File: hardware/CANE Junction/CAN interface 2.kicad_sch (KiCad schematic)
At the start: 20 parts, among them J2 glv, U401 TL432DBZ, U402 TPS7B4254, U403 ISO1044BD, U404 ISOM8600, U405 PUCC33420QRAQRQ1

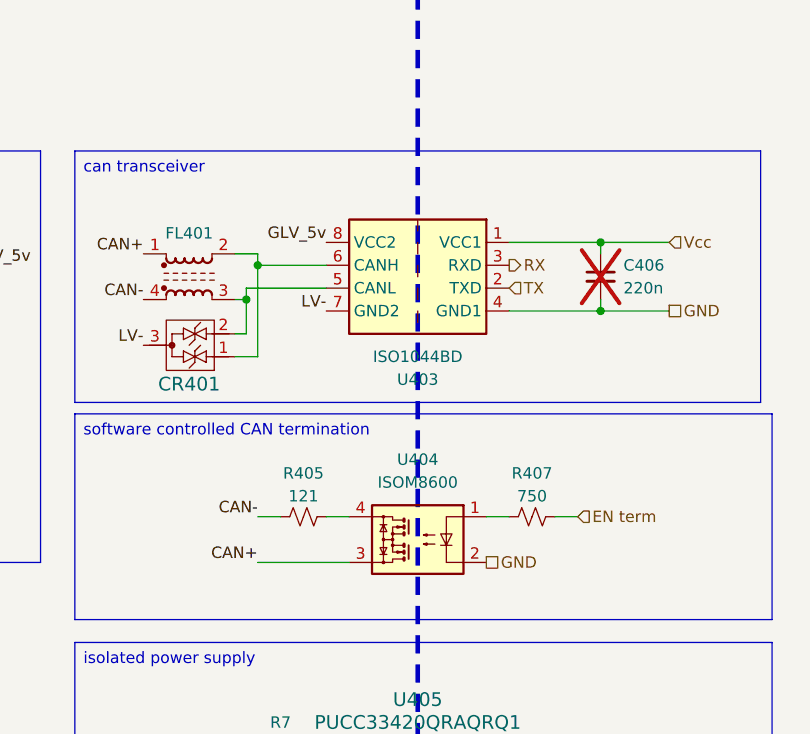
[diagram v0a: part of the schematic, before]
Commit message: transcevier out of stock, swapped out
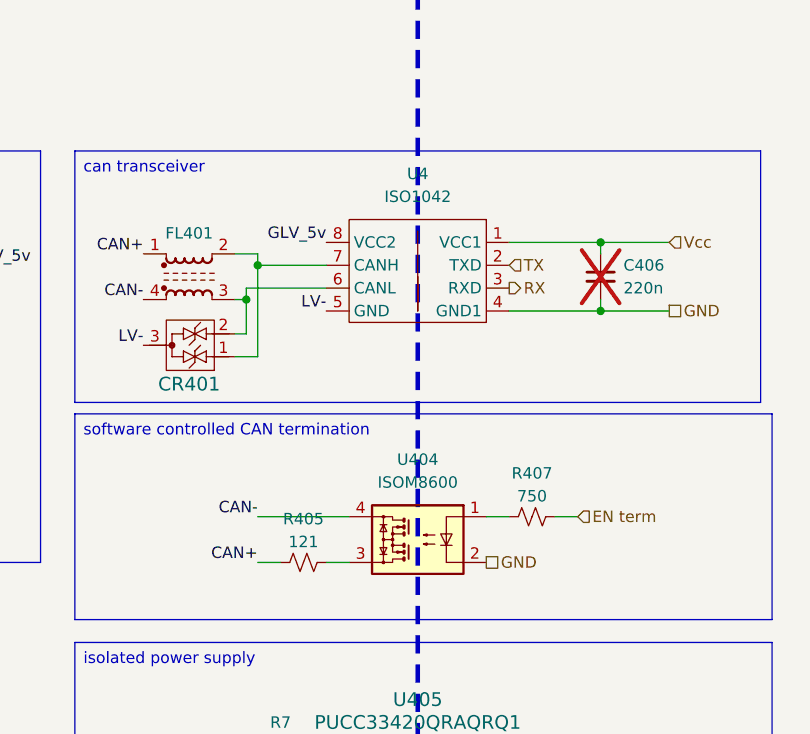
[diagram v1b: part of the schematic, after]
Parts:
- removed U403: ISO1044BD, Package_SO:SOIC-8_5.3x5.3mm_P1.27mm, symbol Interface_CAN_LIN:ISO1044BD
- added U4: ISO1042, Package_SO:SOIC-8_7.5x5.85mm_P1.27mm, symbol zzLocalLibrary:ISO1042
- J2: mouser (none) -> https://www.mouser.com/ProductDetail/Molex/43045-0421?qs=Ue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
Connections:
- net CAN+: now also R405.1; no longer U404.3
- net CAN-: now also U404.4; no longer R405.1
- net GLV_5v: now also U4.8 (VCC2)
- net GND: now also U4.4 (GND1)
- net LV-: now also U4.5 (GND)
- net RX: now also U4.3 (RXD)
- net TX: now also U4.2 (TXD)
- net Vcc: now also U4.1 (VCC1)
- net at R405.2: now also U404.3; no longer U404.4
- net at CR401.2, FL401.3: now also U4.6 (CANL)
- net at CR401.1, FL401.2: now also U4.7 (CANH)
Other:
- moved on the sheet: R405
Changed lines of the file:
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@@
-	(wire
-		(pts
-			(xy 109.22 85.09) (xy 111.76 85.09)
-		)
-		(stroke
-			(width 0)
-			(type default)
-		)
-	)
 	(wire
 		(pts
@@
 	(wire
 		(pts
-			(xy 101.6 85.09) (xy 104.14 85.09)
+			(xy 101.6 85.09) (xy 111.76 85.09)
 		)
 		(stroke
@@
 	(wire
 		(pts
+			(xy 109.22 90.17) (xy 111.76 90.17)
+		)
+		(stroke
+			(width 0)
+			(type default)
+		)
+	)
+	(wire
+		(pts
 			(xy 109.22 120.65) (xy 109.22 123.19)
 		)
@@
 	(wire
 		(pts
-			(xy 101.6 90.17) (xy 111.76 90.17)
+			(xy 101.6 90.17) (xy 104.14 90.17)
 		)
 		(stroke
@@
 	(hierarchical_label "RX"
 		(shape output)
-		(at 129.54 57.15 0)
+		(at 129.54 59.69 0)
 		(effects
 			(font
@@
 	(hierarchical_label "TX"
 		(shape input)
-		(at 129.54 59.69 0)
+		(at 129.54 57.15 0)
 		(effects
 			(font
@@
 	(symbol
 		(lib_id "Device:R_Small_US")
-		(at 106.68 85.09 90)
+		(at 106.68 90.17 90)
 		(unit 1)
 		(body_style 1)
@@
 		(dnp no)
 		(property "Reference" "R405"
-			(at 106.68 80.264 90)
+			(at 106.68 85.344 90)
 			(show_name no)
 			(do_not_autoplace no)
@@
 		)
 		(property "Value" "121"
-			(at 106.68 82.804 90)
+			(at 106.68 87.884 90)
 			(show_name no)
 			(do_not_autoplace no)
@@
 		)
 		(property "Footprint" "Resistor_SMD:R_0805_2012Metric_Pad1.20x1.40mm_HandSolder"
-			(at 106.68 85.09 0)
+			(at 106.68 90.17 0)
 			(hide yes)
 			(show_name no)
@@
 		)
 		(property "Datasheet" ""
-			(at 106.68 85.09 0)
+			(at 106.68 90.17 0)
 			(hide yes)
 			(show_name no)
@@
 		)
 		(property "Description" "Resistor, US symbol"
-			(at 106.68 85.09 0)
+			(at 106.68 90.17 0)
 			(hide yes)
 			(show_name no)
@@
 		)
 		(property "Sim.Device" ""
-			(at 106.68 85.09 0)
+			(at 106.68 90.17 0)
 			(hide yes)
 			(show_name no)
@@
 		)
 		(property "Sim.Type" ""
-			(at 106.68 85.09 0)
+			(at 106.68 90.17 0)
 			(hide yes)
 			(show_name no)
@@
 		)
 		(property "mouser" "https://www.mouser.com/ProductDetail/SEI-Stackpole/RNCP0805FTD121R?qs=sGAEpiMZZMvdGkrng054tyMPH50YnZ95dJmxWK8e%2FBgSyeAIVnAHjA%3D%3D"
-			(at 106.68 85.09 0)
+			(at 106.68 90.17 0)
 			(hide yes)
 			(show_name no)
@@
 		)
 		(property "specs" "121Ohm, 200V, 250mW, 1%, 100ppm, -55C, +155C"
-			(at 106.68 85.09 0)
+			(at 106.68 90.17 0)
 			(hide yes)
 			(show_name no)
@@
 		)
 		(property "unit x1" "0.10"
-			(at 106.68 85.09 0)
+			(at 106.68 90.17 0)
 			(hide yes)
 			(show_name no)
@@
 		)
 		(property "unit x10" "0.012"
-			(at 106.68 85.09 0)
+			(at 106.68 90.17 0)
 			(hide yes)
 			(show_name no)
@@
 		)
 		(property "Sim.Pins" ""
-			(at 106.68 85.09 0)
+			(at 106.68 90.17 0)
 			(hide yes)
 			(show_name no)
@@
 		)
 		(property "note" ""
-			(at 106.68 85.09 0)
+			(at 106.68 90.17 0)
 			(hide yes)
 			(show_name no)
@@
 		)
 		(property "Mouser Part Number" ""
-			(at 106.68 85.09 0)
+			(at 106.68 90.17 0)
 			(hide yes)
 			(show_name no)
@@
 		)
 		(property "Field10" ""
-			(at 106.68 85.09 0)
+			(at 106.68 90.17 0)
 			(hide yes)
 			(show_name no)
@@
 			)
 		)
+		(property "mouser" "https://www.mouser.com/ProductDetail/Molex/43045-0421?qs=UeCeOHRHQebihHCqX%252BVk8Q%3D%3D"
+			(at 29.21 21.59 0)
+			(hide yes)
+			(show_name no)
+			(do_not_autoplace no)
+			(effects
+				(font
+					(size 1.27 1.27)
+				)
+			)
+		)
 		(pin "2"
 		)
@@
 	)
 	(symbol
-		(lib_id "Interface_CAN_LIN:ISO1044BD")
-		(at 119.38 57.15 0)
+		(lib_id "zzLocalLibrary:ISO1042")
+		(at 119.38 50.8 0)
 		(mirror y)
 		(unit 1)
@@
 		(in_pos_files yes)
 		(dnp no)
-		(property "Reference" "U403"
-			(at 119.38 69.85 0)
-			(show_name no)
-			(do_not_autoplace no)
-			(effects
-				(font
-					(size 1.27 1.27)
-				)
-			)
-		)
-		(property "Value" "ISO1044BD"
-			(at 119.38 67.31 0)
-			(show_name no)
-			(do_not_autoplace no)
-			(effects
-				(font
-					(size 1.27 1.27)
-				)
-			)
-		)
-		(property "Footprint" "Package_SO:SOIC-8_5.3x5.3mm_P1.27mm"
-			(at 119.38 67.31 0)
-			(hide yes)
-			(show_name no)
-			(do_not_autoplace no)
-			(effects
-				(font
-					(size 1.27 1.27)
-					(italic yes)
-				)
-			)
-		)
-		(property "Datasheet" "https://www.ti.com/lit/ds/symlink/iso1044.pdf"
-			(at 119.38 69.85 0)
-			(hide yes)
-			(show_name no)
-			(do_not_autoplace no)
-			(effects
-				(font
-					(size 1.27 1.27)
-				)
-			)
-		)
-		(property "Description" "Isolated CAN FD Transceiver, SOIC-8"
-			(at 119.38 57.15 0)
-			(hide yes)
-			(show_name no)
-			(do_not_autoplace no)
-			(effects
-				(font
-					(size 1.27 1.27)
-				)
-			)
+		(property "Reference" "U4"
+			(at 119.38 46.99 0)
+			(show_name no)
+			(do_not_autoplace no)
+			(effects
+				(font
+					(size 1.27 1.27)
+				)
+			)
+		)
+		(property "Value" "ISO1042"
+			(at 119.38 49.53 0)
+			(show_name no)
+			(do_not_autoplace no)
+			(effects
+				(font
+					(size 1.27 1.27)
+				)
+			)
+		)
+		(property "Footprint" "Package_SO:SOIC-8_7.5x5.85mm_P1.27mm"
+			(at 119.38 50.8 0)
+			(hide yes)
+			(show_name no)
+			(do_not_autoplace no)
+			(effects
+				(font
+					(size 1.27 1.27)
+				)
+			)
+		)
+		(property "Datasheet" "https://www.ti.com/lit/ds/symlink/iso1042-q1.pdf"
+			(at 119.38 50.8 0)
+			(hide yes)
+			(show_name no)
+			(do_not_autoplace no)
+			(effects
+				(font
+					(size 1.27 1.27)
+				)
+			)
+		)
+		(property "Description" "isolated can transcevier, 1500Vdc, 5M, CAN-FD"
+			(at 119.38 50.8 0)
+			(hide yes)
+			(show_name no)
+			(do_not_autoplace no)
+			(effects
+				(font
+					(size 1.27 1.27)
+				)
+			)
+		)
+		(property "mouser" "https://www.mouser.com/ProductDetail/Texas-Instruments/ISO1042BQDWVRQ1?qs=byeeYqUIh0NmbePKADUcRQ%3D%3D"
+			(at 119.38 50.8 0)
+			(hide yes)
+			(show_name no)
+			(do_not_autoplace no)
+			(effects
+				(font
+					(size 1.27 1.27)
+				)
+			)
+		)
+		(pin "6"
+		)
+		(pin "4"
+		)
+		(pin "5"
+		)
+		(pin "8"
+		)
+		(pin "2"
 		)
 		(pin "3"
 		)
-		(pin "4"
+		(pin "7"
 		)
 		(pin "1"
-		)
-		(pin "8"
-		)
-		(pin "6"
-		)
-		(pin "7"
-		)
-		(pin "2"
-		)
-		(pin "5"
 		)
 		(instances
 			(project "CANE Junction"
 				(path "/20ac6af0-79b5-4ba6-aad3-75081d02c913/77ba9f55-a932-4615-96e7-79448df1d300"
-					(reference "U403")
+					(reference "U4")
 					(unit 1)
 				)

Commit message: mmm
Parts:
- removed C401, C402, C403, C406, C407: 220n, Capacitor_SMD:C_0805_2012Metric_Pad1.18x1.45mm_HandSolder, symbol Device:C_Small
- removed C404, C405: 22u, Capacitor_SMD:C_0805_2012Metric_Pad1.18x1.45mm_HandSolder, symbol Device:C_Small
- removed CR401: ESD2CAN36DBZRQ1, Package_TO_SOT_SMD:TSOT-23_HandSoldering, symbol zzLocalLibrary:ESD2CAN36DBZRQ1
- removed D401: TS4148, Diode_SMD:D_0805_2012Metric_Pad1.15x1.40mm_HandSolder, symbol Device:D_Small
- removed FL401: Choke_CommonMode_FerriteCore_1243, zzLocalLibraries-Footprints:L_CommonModeChoke_Coilcraft_1812CAN, symbol Filter:Choke_CommonMode_FerriteCore_1243
- removed J2: glv, Connector_Molex:Molex_Micro-Fit_3.0_43045-0400_2x02_P3.00mm_Horizontal, symbol Connector_Generic:Conn_01x04
- removed R405: 121, Resistor_SMD:R_0805_2012Metric_Pad1.20x1.40mm_HandSolder, symbol Device:R_Small_US
- removed R407: 750, Resistor_SMD:R_0805_2012Metric_Pad1.20x1.40mm_HandSolder, symbol Device:R_Small_US
- removed R7: 40.2k, Resistor_SMD:R_0805_2012Metric_Pad1.20x1.40mm_HandSolder, symbol Device:R_Small_US
- removed RN2: 56K, zzLocalLibraries-Footprints:R_array_YCJ164_4, symbol Device:R_Pack04_SIP_Split
- removed U4: ISO1042, Package_SO:SOIC-8_7.5x5.85mm_P1.27mm, symbol zzLocalLibrary:ISO1042
- removed U401: TL432DBZ, Package_TO_SOT_SMD:SOT-23-3, symbol Reference_Voltage:TL432DBZ
- removed U402: TPS7B4254, Package_SO:Texas_R-PDSO-G8_EP2.95x4.9mm_Mask2.4x3.1mm, symbol zzLocalLibrary:TPS7B4252
- removed U404: ISOM8600, zzLocalLibraries-Footprints:SOIC4_DFG_TEX-M, symbol zzLocalLibrary:ISOM8600
- removed U405: PUCC33420QRAQRQ1, zzLocalLibraries-Footprints:VSON-FCRLF12_RAQ_TEX, symbol zzLocalLibrary:PUCC33420QRAQRQ1
- added C201, C202: 470n, Capacitor_SMD:C_0805_2012Metric_Pad1.18x1.45mm_HandSolder, symbol Device:C_Small
- added C203, C207, C208: 220n, Capacitor_SMD:C_0805_2012Metric_Pad1.18x1.45mm_HandSolder, symbol Device:C_Small
- added C204, C205, C206: 22u, Capacitor_SMD:C_0805_2012Metric_Pad1.18x1.45mm_HandSolder, symbol Device:C_Small
- added CR201: ESD2CAN36DBZRQ1, Package_TO_SOT_SMD:TSOT-23_HandSoldering, symbol zzLocalLibrary:ESD2CAN36DBZRQ1
- added D201, D202: ES1D, Diode_SMD:D_SMA, symbol Device:D_Schottky_Small
- added FL201: Choke_CommonMode_FerriteCore_1243, Inductor_SMD:L_CommonMode_Wurth_WE-CNSW-1206, symbol Filter:Choke_CommonMode_FerriteCore_1243
- added J201: glv, Connector_Molex:Molex_Micro-Fit_3.0_43045-0400_2x02_P3.00mm_Horizontal, symbol Connector_Generic:Conn_01x04
- added L201: 10u, Inductor_SMD:L_1210_3225Metric_Pad1.42x2.65mm_HandSolder, symbol Device:L_Small
- added R201: 121, Resistor_SMD:R_0805_2012Metric_Pad1.20x1.40mm_HandSolder, symbol Device:R_Small_US
- added R202: 750, Resistor_SMD:R_0805_2012Metric_Pad1.20x1.40mm_HandSolder, symbol Device:R_Small_US
- added RN201: 20k, zzLocalLibraries-Footprints:R_array_EXB2HV_8, symbol Device:R_Pack08_Split
- added TP201: TestPoint, TestPoint:TestPoint_Pad_D1.0mm, symbol Connector:TestPoint
- added U201: AP64060ZQ, Package_TO_SOT_SMD:TSOT-23-6, symbol zzLocalLibrary:AP64060ZQ
- added U202: MCP2542FDxMF, Package_SO:SOIC-8_3.9x4.9mm_P1.27mm, symbol Interface_CAN_LIN:MCP2542FDxMF
- added U203: ISO7721D, Package_SO:SOIC-8_3.9x4.9mm_P1.27mm, symbol Isolator:ISO7721D
- added U204: ISOM8600, zzLocalLibraries-Footprints:SOIC4_DFG_TEX-M, symbol zzLocalLibrary:ISOM8600
- added U205: PUCC33420QRAQRQ1, zzLocalLibraries-Footprints:VSON-FCRLF12_RAQ_TEX, symbol zzLocalLibrary:PUCC33420QRAQRQ1
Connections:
- net 5v: now also C206.2, C208.2, U205.7 (SEL), U205.8 (VCC)
- net CAN+: now also FL201.4, J201.3 (Pin_3), U204.4
- net CAN-: now also FL201.1, J201.4 (Pin_4), R201.1
- net EN term: now also R202.2
- net GLV_5v: now also C204.1, C205.1, L201.1, RN201.16 (R1.2), RN201.9 (R8.2), TP201.1, U202.3 (VDD), U202.5 (VIO), U203.1 (VCC1), U205.2 (VINP)
- net GND: now also C206.1, C207.2, C208.1, U203.5 (GND2), U204.2, U205.10 (GNDS), U205.11 (GNDS), U205.12 (GNDS), U205.9 (GNDS)
- net LV+: now also D201.2 (A), J201.2 (Pin_2)
- net LV-: now also C201.2, C202.2, C204.2, C205.2, CR201.3, D202.2 (A), J201.1 (Pin_1), RN201.5 (R5.1), U201.2 (GND), U202.2 (VSS), U202.8 (STBY), U202.9 (VSS), U203.4 (GND1), U205.3 (GNDP), U205.4 (GNDP), U205.5 (GNDP), U205.6 (GNDP)
- net RX: now also U203.6 (OUTB)
- net TX: now also U203.7 (INA)
- net Vcc: now also C207.1, U203.8 (VCC2)
- new net: RN201.8 (R8.1), U205.1 (EN/FLT)
- new net: RN201.1 (R1.1), RN201.15 (R2.2)
- new net: C201.1, C202.1, D201.1 (K), U201.4 (EN), U201.5 (Vin)
- new net: RN201.14 (R3.2), RN201.2 (R2.1)
- new net: RN201.13 (R4.2), RN201.3 (R3.1)
- new net: RN201.12 (R5.2), RN201.4 (R4.1), U201.3 (FB)
- new net: R202.1, U204.1
- new net: CR201.1, FL201.2, U202.6 (CANL)
- new net: CR201.2, FL201.3, U202.7 (CANH)
- new net: R201.2, U204.3
- new net: C203.1, U201.1 (BST)
- new net: C203.2, D202.1 (K), L201.2, U201.6 (SW)
- new net: U202.1 (TXD), U203.2 (OUTA)
- new net: U202.4 (RXD), U203.3 (INB)
- no-connect marks 2 -> 0

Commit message: tmb pci technology
doner motherboard generator
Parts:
- removed D202: ES1D, Diode_SMD:D_SMA, symbol Device:D_Schottky_Small
- removed U202: MCP2542FDxMF, Package_SO:SOIC-8_3.9x4.9mm_P1.27mm, symbol Interface_CAN_LIN:MCP2542FDxMF
- removed U203: ISO7721D, Package_SO:SOIC-8_3.9x4.9mm_P1.27mm, symbol Isolator:ISO7721D
- removed U204: ISOM8600, zzLocalLibraries-Footprints:SOIC4_DFG_TEX-M, symbol zzLocalLibrary:ISOM8600
- removed U205: PUCC33420QRAQRQ1, zzLocalLibraries-Footprints:VSON-FCRLF12_RAQ_TEX, symbol zzLocalLibrary:PUCC33420QRAQRQ1
- added D202: TS4148, Diode_SMD:D_0805_2012Metric_Pad1.15x1.40mm_HandSolder, symbol Device:D_Small
- added unit 7 of RN201
- added unit 6 of RN201
- added U202: ISO1044BD, Package_SO:SOIC-8_5.3x6.2mm_P1.27mm, symbol Interface_CAN_LIN:ISO1044BD
- added U203: ISOM8600, zzLocalLibraries-Footprints:SOIC4_DFG_TEX-M, symbol zzLocalLibrary:ISOM8600
- added U204: PUCC33420QRAQRQ1, zzLocalLibraries-Footprints:VSON-FCRLF12_RAQ_TEX, symbol zzLocalLibrary:PUCC33420QRAQRQ1
- added U205: NCP163ASN330T1G, Package_TO_SOT_SMD:SOT-23-5_HandSoldering, symbol Regulator_Linear:NCP163ASN330T1G
- CR201: mouser (none) -> https://www.mouser.com/ProductDetail/Texas-Instruments/ESD2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
- J201: mouser https://www.mouser.com/ProductDetail/Molex/43045-0421?qs=Ue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 -> https://www.mouser.com/ProductDetail/Molex/43045-0400?qs=Ue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
- TP201: now not fitted; now left out of the parts list
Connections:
- net CAN+: now also FL201.1, U203.3; no longer FL201.4
- net CAN-: now also FL201.4, R201.2; no longer FL201.1, R201.1
- net GLV_5v: now also RN201.12 (R5.2), RN201.8 (R8.1), U202.8 (VCC2), U204.2 (VINP); no longer RN201.16 (R1.2), RN201.9 (R8.2)
- net GND: now also U202.4 (GND1), U203.2, U204.10 (GNDS), U204.11 (GNDS), U204.12 (GNDS), U204.9 (GNDS), U205.2 (GND)
- net LV-: now also RN201.1 (R1.1), D202.2 (A), U202.7 (GND2), U204.3 (GNDP), U204.4 (GNDP), U204.5 (GNDP), U204.6 (GNDP); no longer RN201.5 (R5.1)
- net RX: now also U202.3 (RXD)
- net TX: now also U202.2 (TXD)
- net Vcc: now also U202.1 (VCC1)
- net at RN201.15 (R2.2): now also RN201.16 (R1.2), U201.3 (FB); no longer RN201.1 (R1.1)
- net at RN201.14 (R3.2): now also RN201.13 (R4.2); no longer RN201.2 (R2.1)
- net at RN201.3 (R3.1): now also RN201.2 (R2.1); no longer RN201.13 (R4.2)
- net at R202.1: now also U203.1
- net C_N: now reaches CR201.1
- net C_N: now also FL201.3, U202.5 (CANL); no longer FL201.2
- net C_P: now reaches CR201.2
- net C_P: now also FL201.2, U202.6 (CANH); no longer FL201.3
- net at C203.2, L201.2, U201.6 (SW): now also D202.1 (K)
- net 5v: no longer names the net of C206.2, C208.2
- net 5v: now also U204.7 (SEL), U204.8 (VCC), U205.1 (VIN), U205.3 (EN)
- new net: R201.1, U203.4
- new net: RN201.9 (R8.2), U204.1 (EN/FLT)
- new net: RN201.4 (R4.1), RN201.5 (R5.1)
- new net 3v3: U205.5 (VOUT)
- no-connect marks 0 -> 4
